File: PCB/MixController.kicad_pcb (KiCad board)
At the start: 2 copper layers, 150.2 x 114.3 mm, 120 parts, among them J11 B5B-XH-A(LF)(SN), J13 B8B-XH-A(LF)(SN), J2 B2B-XH-A(LF)(SN), J7 B3B-XH-A(LF)(SN), J9 B2B-XH-A(LF)(SN), J91 B4B-XH-A(LF)(SN), J94 0705430001, J95 B8B-XH-A(LF)(SN), J97 B4B-PH-K-S(LF)(SN), Q1 Q_NMOS_GDS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

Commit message: Continue Layout
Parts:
- added PS1: TMR_6-7215WIR, Local:TRACO_TMR_6, F.Cu at (187.3, 88.3)
- added PS2: RSDW20H-05, Local:RSDW20_H, F.Cu at (142.2, 58.4)
- added U2: Adafruit_1096, Local:Adafruit_1096, F.Cu at (214.0, 121.9)
- added U3: BOB-12009, Package_DIP:DIP-12_W10.16mm, F.Cu at (200.7, 63.5)
- added U4: BOB-12009, Package_DIP:DIP-12_W10.16mm, F.Cu at (96.5, 63.5)
- added U6: HSCDLNN001PDAA3, Local:HoneyWell_LN, F.Cu at (101.0, 90.8)
- moved R6 25.5 mm to (190.5, 45.7), turned to 0 degrees
- moved R2 20.8 mm to (179.1, 68.6), turned to 0 degrees
- moved R7 5.68 mm to (86.4, 45.7)
- moved R4 3.59 mm to (175.3, 132.1)
- moved R3 1.27 mm to (172.7, 128.3)
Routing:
- net /HARDENER_INPUT_A: track 0.00 -> 145.2 mm, vias 0 -> 2
- net /HARDENER_INPUT_B: track 0.00 -> 140.2 mm, vias 0 -> 2
- net /HARDENER_ENABLE: track 0.00 -> 44.5 mm
- net Net-(J84-Pad1): track 40.5 -> 1.50 mm
- net Net-(J83-Pad1): track 37.0 -> 0.00 mm
- net Net-(J13-Pad5): track 0.00 -> 19.8 mm
- net Net-(J95-Pad5): track 0.00 -> 19.8 mm
- net Net-(J13-Pad6): track 0.00 -> 19.8 mm
- net Net-(J95-Pad6): track 0.00 -> 19.8 mm
- net /HARDENER_HLFB: track 0.00 -> 19.5 mm
- net Net-(J95-Pad8): track 0.00 -> 17.9 mm
- net Net-(J13-Pad8): track 0.00 -> 17.9 mm
- net Net-(J95-Pad7): track 0.00 -> 17.9 mm
- net Net-(J13-Pad7): track 0.00 -> 17.9 mm
- net /USER_BUTTON: track 84.8 -> 86.3 mm
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
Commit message: Continue Layout
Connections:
- JP4 pad 1: /PAIL_SNS -> /PRESS_SNS
- JP5 pad 1: /PRESS_SNS -> /PAIL_SNS
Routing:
- net /RESIN_HLFB: track 0.00 -> 108.8 mm, vias 0 -> 4
- net /RESIN_ENABLE: track 0.00 -> 102.5 mm, vias 0 -> 4
- net /RESIN_INPUT_B: track 0.00 -> 101.2 mm, vias 0 -> 2
- net /HARDENER_HLFB: track 19.5 -> 120.2 mm, vias 0 -> 4
- net /RESIN_INPUT_A: track 0.00 -> 93.0 mm, vias 0 -> 2
- net /HARDENER_ENABLE: track 44.5 -> 130.8 mm, vias 0 -> 4
- net /PRESS_SNS: track 0.00 -> 54.8 mm
- net Net-(J84-Pad1): track 1.50 -> 41.8 mm
- net Net-(J83-Pad1): track 0.00 -> 37.0 mm
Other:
- board text added: "+5V"
- board text added: "3V3"
- board text added: "GND"

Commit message: Update Board Profile
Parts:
- moved PS2 138.5 mm to (5.71, 81.9)
- moved Q1 95.7 mm to (268.0, 46.4)
- moved R2 91.1 mm to (269.9, 61.6)
- moved PS1 66.7 mm to (121.3, 78.7), turned to 270 degrees
- moved J2 21.6 mm to (170.8, 57.1)
- moved J7 21.6 mm to (150.5, 57.1)
- moved J94 21.6 mm to (135.3, 57.1)
- moved JP10 10.9 mm to (146.1, 140.3)
- moved JP11 10.9 mm to (148.6, 140.3)
- moved JP19 10.9 mm to (128.3, 144.1)
- moved JP20 10.9 mm to (128.3, 146.7)
- moved JP23 10.9 mm to (128.3, 154.3)
- moved JP7 10.9 mm to (138.4, 140.3)
- moved JP8 10.9 mm to (141.0, 140.3)
- moved R9 10.9 mm to (181.6, 130.2)
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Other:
- board size 150.2 x 114.3 mm -> 150.2 x 127 mm

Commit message: Update PCB Layout
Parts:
- moved PS2 108.6 mm to (114.3, 80.0)
- moved Q1 102.9 mm to (169.5, 76.2), turned to 90 degrees
- moved R2 93.2 mm to (177.8, 76.2), turned to 270 degrees
- moved PS1 36.7 mm to (156.8, 87.6), turned to 0 degrees
- moved U6 6.35 mm to (97.2, 105.4)
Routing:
- net +5V: track 0.00 -> 486.5 mm, vias 0 -> 3
- net +3V3: track 0.00 -> 362.9 mm, vias 0 -> 6
- net +72V: track 0.00 -> 39.7 mm
- net +24V: track 0.00 -> 37.7 mm
- net Net-(J2-Pad2): track 0.00 -> 19.6 mm
- net /RESIN_HLFB: track 108.8 -> 121.5 mm
- net /RESIN_INPUT_B: track 101.2 -> 113.9 mm
- net /RESIN_INPUT_A: track 93.0 -> 105.7 mm
- net /RESIN_ENABLE: track 102.5 -> 115.2 mm
- net /HARDENER_INPUT_B: track 140.2 -> 152.9 mm
- net /HARDENER_INPUT_A: track 145.2 -> 157.9 mm
- net /HARDENER_ENABLE: track 130.8 -> 143.4 mm
- net /HARDENER_HLFB: track 120.2 -> 132.5 mm
- net /PRESS_SNS: track 54.8 -> 45.8 mm
- net /PUMP_EN: track 0.00 -> 8.26 mm
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
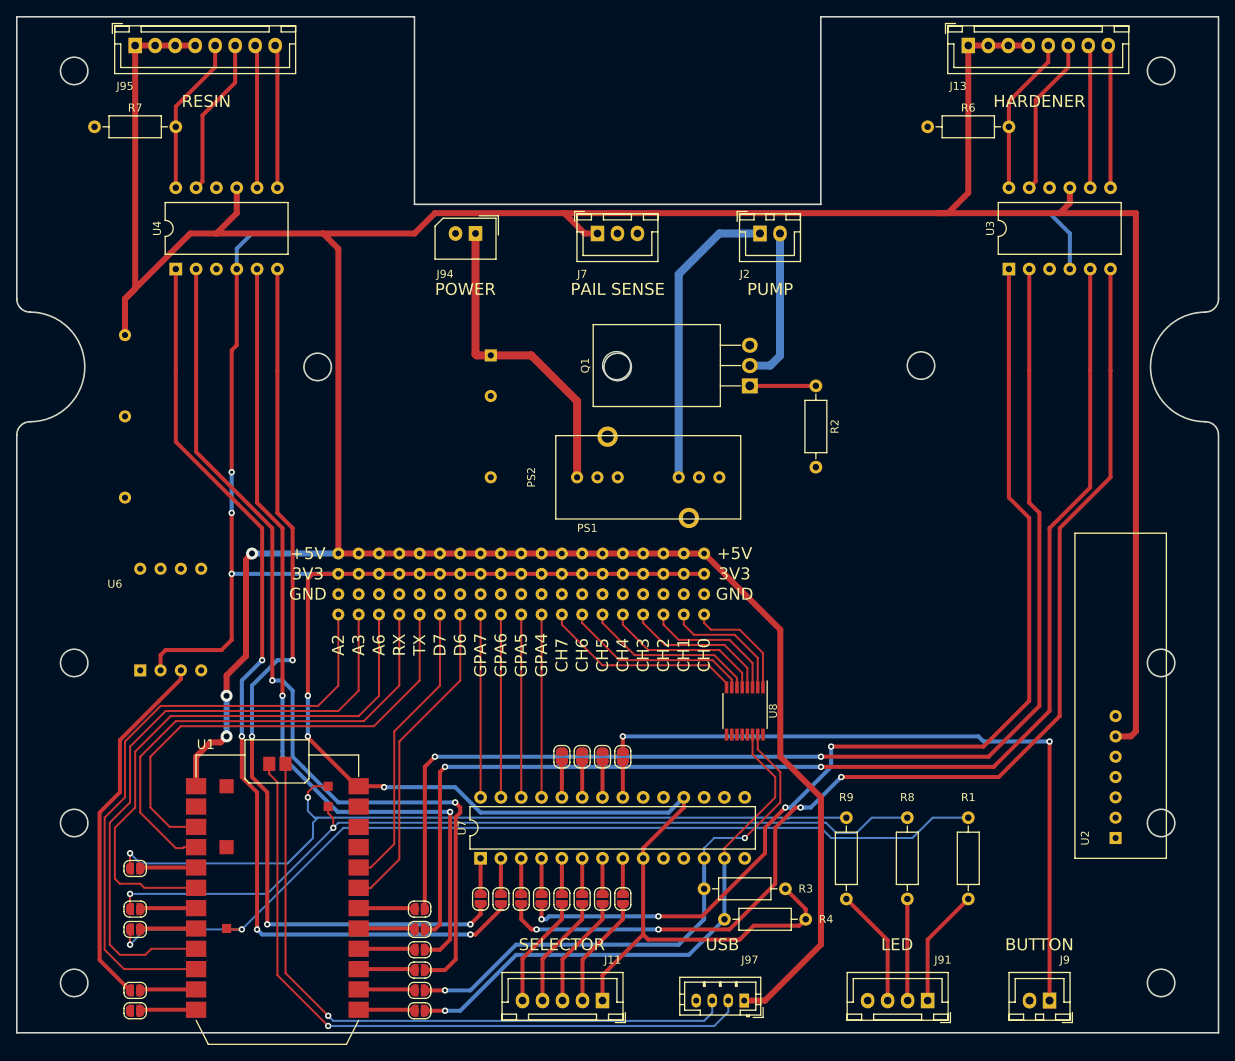
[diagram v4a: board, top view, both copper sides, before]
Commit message: Add indicator leds, chime speaker, update layout
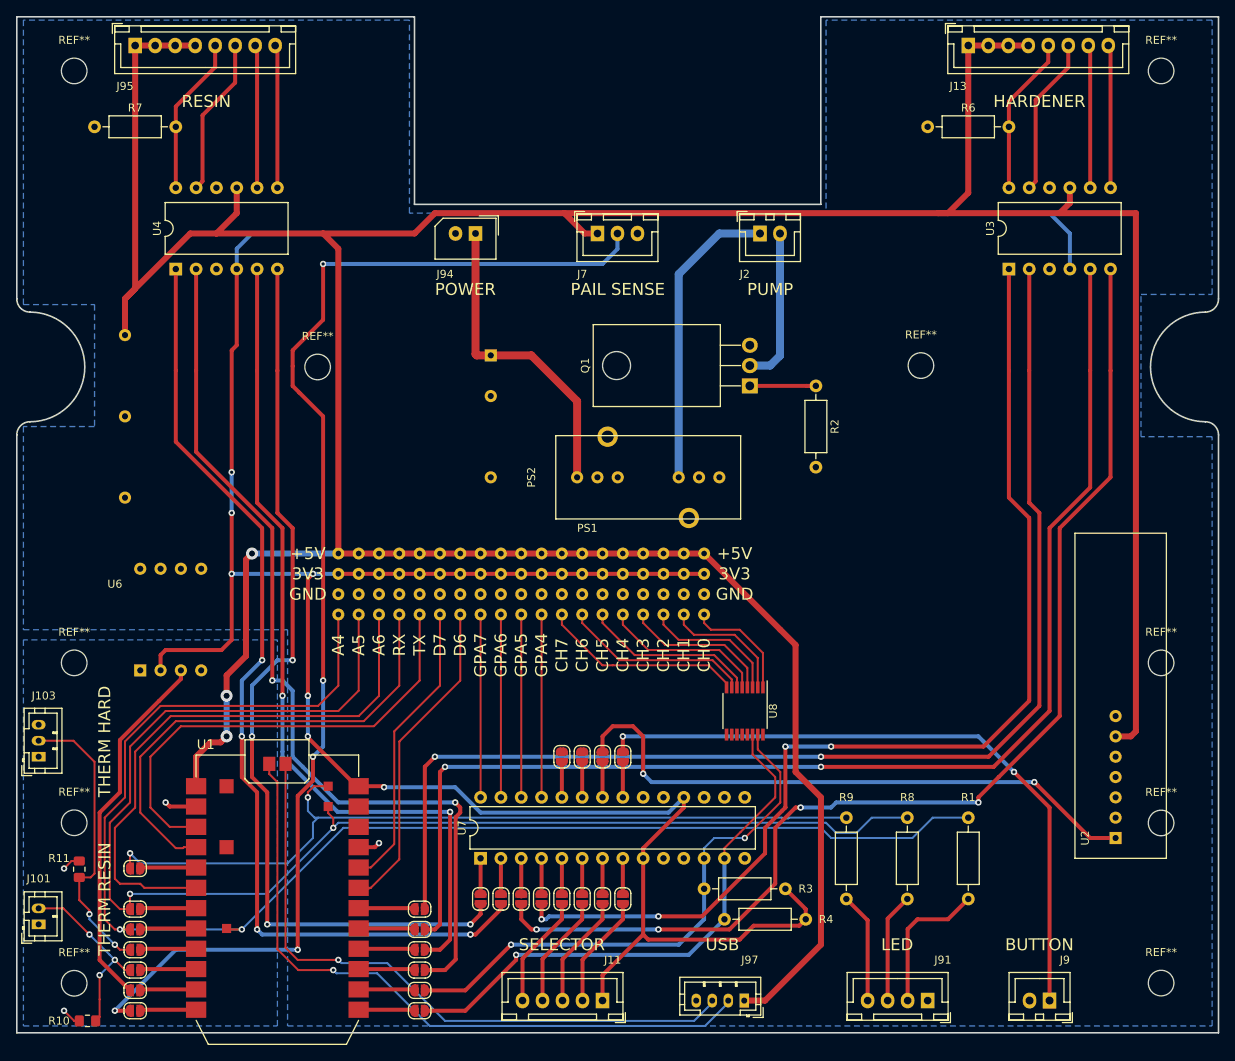
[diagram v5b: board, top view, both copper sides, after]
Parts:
- added J101: B2B-PH-K-S(LF)(SN), Connector_JST:JST_PH_B2B-PH-K_1x02_P2.00mm_Vertical, F.Cu at (80.6, 143.5)
- added J103: B3B-PH-K-S(LF)(SN), Connector_JST:JST_PH_B3B-PH-K_1x03_P2.00mm_Vertical, F.Cu at (80.6, 122.6)
- added JP24: ~, Jumper:SolderJumper-2_P1.3mm_Open_RoundedPad1.0x1.5mm, F.Cu at (92.7, 146.7)
- added JP25: ~, Jumper:SolderJumper-2_P1.3mm_Open_RoundedPad1.0x1.5mm, F.Cu at (92.7, 149.2)
- added R10: 10K .01%, Resistor_SMD:R_0805_2012Metric_Pad1.15x1.40mm_HandSolder, F.Cu at (86.8, 155.6)
- added R11: 10K .01%, Resistor_SMD:R_0805_2012Metric_Pad1.15x1.40mm_HandSolder, F.Cu at (85.7, 136.6)
- added REF**: MountingHole_3.2mm_M3_ISO7380, MountingHole:MountingHole_3.2mm_M3_ISO7380, F.Cu at (115.5, 73.8)
- added REF**: MountingHole_3.2mm_M3_ISO7380, MountingHole:MountingHole_3.2mm_M3_ISO7380, F.Cu at (85.1, 150.9)
- added REF**: MountingHole_3.2mm_M3_ISO7380, MountingHole:MountingHole_3.2mm_M3_ISO7380, F.Cu at (221.0, 110.8)
- added REF**: MountingHole_3.2mm_M3_ISO7380, MountingHole:MountingHole_3.2mm_M3_ISO7380, F.Cu at (221.0, 130.8)
- added REF**: MountingHole_3.2mm_M3_ISO7380, MountingHole:MountingHole_3.2mm_M3_ISO7380, F.Cu at (221.0, 150.9)
- added REF**: MountingHole_3.2mm_M3_ISO7380, MountingHole:MountingHole_3.2mm_M3_ISO7380, F.Cu at (190.9, 73.7)
- added REF**: MountingHole_3.2mm_M3_ISO7380, MountingHole:MountingHole_3.2mm_M3_ISO7380, F.Cu at (221.0, 36.8)
- added REF**: MountingHole_3.2mm_M3_ISO7380, MountingHole:MountingHole_3.2mm_M3_ISO7380, F.Cu at (85.1, 36.8)
- added REF**: MountingHole_3.2mm_M3_ISO7380, MountingHole:MountingHole_3.2mm_M3_ISO7380, F.Cu at (85.1, 110.8)
- added REF**: MountingHole_3.2mm_M3_ISO7380, MountingHole:MountingHole_3.2mm_M3_ISO7380, F.Cu at (85.1, 130.8)
- U7: value MCP23017 -> MCP23017_SP
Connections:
- J45 pad 1: Net-(J45-Pad1) -> /STATUS_LED_G
- J46 pad 1: Net-(J46-Pad1) -> /STATUS_LED_R
- J91 pad 1: Net-(J91-Pad1) -> +3V3
- J91 pad 4: GND -> Net-(J91-Pad4)
- R1 pad 2: Net-(J91-Pad1) -> Net-(J91-Pad2)
- R8 pad 2: Net-(J91-Pad2) -> Net-(J91-Pad3)
- R9 pad 2: Net-(J91-Pad3) -> Net-(J91-Pad4)
- U1 pad 10: Net-(J46-Pad1) -> Net-(JP25-Pad2)
- U1 pad 9: Net-(J45-Pad1) -> Net-(JP24-Pad2)
- U7 pad 11: (no net) -> Net-(U7-Pad11)
- U7 pad 14: (no net) -> Net-(U7-Pad14)
- U8 pad 11: Net-(U8-Pad11) -> GND
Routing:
- net /PAIL_SNS: track 0.00 -> 157.6 mm, vias 0 -> 5
- net Net-(J45-Pad1): track 78.4 -> 0.00 mm
- net Net-(J46-Pad1): track 78.0 -> 0.00 mm
- net /USER_REMOTE: track 0.00 -> 75.1 mm, vias 0 -> 2
- net /STATUS_LED_G: track 107.0 -> 171.1 mm
- net /STATUS_LED_R: track 116.3 -> 180.3 mm
- net /THERM_HARDENER: track 0.00 -> 36.6 mm, vias 0 -> 2
- net /THERM_RESIN: track 0.00 -> 23.2 mm, vias 0 -> 3
- net Net-(J91-Pad1): track 14.8 -> 0.00 mm
- net Net-(J91-Pad4): track 0.00 -> 13.8 mm
- net GND: track 0.00 -> 11.5 mm, vias 0 -> 4
- net Net-(JP24-Pad2): track 0.00 -> 7.00 mm
- net Net-(JP25-Pad2): track 0.00 -> 7.00 mm
- net Net-(J91-Pad2): track 12.7 -> 18.1 mm
- net /USER_BUTTON: track 87.9 -> 83.0 mm
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- added copper zone on B.Cu, net GND
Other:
- outline, holes or cut-outs redrawn
- board text added: "A4"
- board text added: "A5"
- board text added: "THERM HARD"
- board text added: "THERM RESIN"
- board text removed: "A2"
- board text removed: "A3"

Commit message: update schematic per ECN Maxx 5
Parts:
- added C1: 0.1u, Capacitor_SMD:C_0805_2012Metric_Pad1.15x1.40mm_HandSolder, F.Cu at (50.5, 146.1)
- added C2: 0.1u, Capacitor_SMD:C_0805_2012Metric_Pad1.15x1.40mm_HandSolder, F.Cu at (62.8, 136.2)
- added C3: 0.1u, Capacitor_SMD:C_0805_2012Metric_Pad1.15x1.40mm_HandSolder, F.Cu at (50.5, 148.0)
- added C4: 0.1u, Capacitor_SMD:C_0805_2012Metric_Pad1.15x1.40mm_HandSolder, F.Cu at (59.0, 139.3)
- added C5: 470u, Capacitor_SMD:C_0805_2012Metric_Pad1.15x1.40mm_HandSolder, F.Cu at (54.3, 146.1)
- added D10: STEP_HARD, LED_SMD:LED_0805_2012Metric_Pad1.15x1.40mm_HandSolder, F.Cu at (47.0, 113.6)
- added D11: STEP_RESIN, LED_SMD:LED_0805_2012Metric_Pad1.15x1.40mm_HandSolder, F.Cu at (39.4, 119.7)
- added D2: +72V, LED_SMD:LED_0805_2012Metric_Pad1.15x1.40mm_HandSolder, F.Cu at (39.4, 111.5)
- added D3: +5V, LED_SMD:LED_0805_2012Metric_Pad1.15x1.40mm_HandSolder, F.Cu at (39.4, 113.6)
- added D4: +24V, LED_SMD:LED_0805_2012Metric_Pad1.15x1.40mm_HandSolder, F.Cu at (43.2, 111.5)
- added D5: EN_HARD, LED_SMD:LED_0805_2012Metric_Pad1.15x1.40mm_HandSolder, F.Cu at (39.4, 115.6)
- added D6: EN_RESIN, LED_SMD:LED_0805_2012Metric_Pad1.15x1.40mm_HandSolder, F.Cu at (43.2, 113.6)
- added D7: PUMP, LED_SMD:LED_0805_2012Metric_Pad1.15x1.40mm_HandSolder, F.Cu at (47.0, 111.5)
- added D8: LIQ_RESIN, LED_SMD:LED_0805_2012Metric_Pad1.15x1.40mm_HandSolder, F.Cu at (39.4, 117.6)
- added D9: LIQ_HARD, LED_SMD:LED_0805_2012Metric_Pad1.15x1.40mm_HandSolder, F.Cu at (43.2, 115.6)
- added J104: B2B-XH-A(LF)(SN), Connector_JST:JST_XH_B02B-XH-A_1x02_P2.50mm_Vertical, F.Cu at (51.6, 141.2)
- added JP26: ~, Jumper:SolderJumper-2_P1.3mm_Open_RoundedPad1.0x1.5mm, F.Cu at (50.3, 152.2)
- added JP27: ~, Jumper:SolderJumper-2_P1.3mm_Open_RoundedPad1.0x1.5mm, F.Cu at (58.8, 143.5)
- added Q2: Q_NMOS_GDS, Package_TO_SOT_THT:TO-220-3_Horizontal_TabDown, F.Cu at (40.8, 155.0)
- added R12: 23k, Resistor_SMD:R_0805_2012Metric_Pad1.15x1.40mm_HandSolder, F.Cu at (50.7, 111.5)
- added R13: 1k, Resistor_SMD:R_0805_2012Metric_Pad1.15x1.40mm_HandSolder, F.Cu at (43.1, 117.6)
- added R14: 7k, Resistor_SMD:R_0805_2012Metric_Pad1.15x1.40mm_HandSolder, F.Cu at (46.9, 115.5)
- added R15: 100K, Resistor_SMD:R_0805_2012Metric_Pad1.15x1.40mm_HandSolder, F.Cu at (49.7, 136.8)
- added R16: 1k, Resistor_SMD:R_0805_2012Metric_Pad1.15x1.40mm_HandSolder, F.Cu at (50.7, 113.4)
- added R17: 1k, Resistor_SMD:R_0805_2012Metric_Pad1.15x1.40mm_HandSolder, F.Cu at (43.1, 119.5)
- added R18: 7k, Resistor_SMD:R_0805_2012Metric_Pad1.15x1.40mm_HandSolder, F.Cu at (46.9, 117.5)
- added R19: 10k, Resistor_SMD:R_0805_2012Metric_Pad1.15x1.40mm_HandSolder, F.Cu at (59.0, 141.2)
- added R20: 10k, Resistor_SMD:R_0805_2012Metric_Pad1.15x1.40mm_HandSolder, F.Cu at (62.8, 138.2)
- added R21: 470, Resistor_SMD:R_0805_2012Metric_Pad1.15x1.40mm_HandSolder, F.Cu at (50.5, 150.0)
- added R22: 470, Resistor_SMD:R_0805_2012Metric_Pad1.15x1.40mm_HandSolder, F.Cu at (66.6, 136.2)
- added R23: 1k, Resistor_SMD:R_0805_2012Metric_Pad1.15x1.40mm_HandSolder, F.Cu at (50.7, 115.5)
- added R24: 1k, Resistor_SMD:R_0805_2012Metric_Pad1.15x1.40mm_HandSolder, F.Cu at (46.9, 119.4)
- added TP1: SCL, TestPoint:TestPoint_THTPad_D1.5mm_Drill0.7mm, F.Cu at (53.7, 148.3)
- added TP2: SDA, TestPoint:TestPoint_THTPad_D1.5mm_Drill0.7mm, F.Cu at (57.4, 146.4)
- J38: value ~ -> B5B-PH-K-S(LF)(SN); footprint Local:ConnectorPoint_THT_D1.5mm_Drill-0.7mm -> Connector_JST:JST_PH_B5B-PH-K_1x05_P2.00mm_Vertical
- J55: value ~ -> PHR-5
- J67: value ~ -> B6B-PH-K-S(LF)(SN); footprint Local:ConnectorPoint_THT_D1.5mm_Drill-0.7mm -> Connector_JST:JST_PH_B6B-PH-K_1x06_P2.00mm_Vertical
- J71: value ~ -> PHR-6
- R10, R11: value 10K .01% -> 5K .01%
- R2: footprint Resistor_THT:R_Axial_DIN0207_L6.3mm_D2.5mm_P10.16mm_Horizontal -> Resistor_SMD:R_0805_2012Metric_Pad1.15x1.40mm_HandSolder
- moved J67 108.7 mm to (36.1, 85.4), turned to 0 degrees
- moved J38 107.6 mm to (36.1, 91.0), turned to 0 degrees
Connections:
- net /HARDENER_INPUT_A renamed /HARDENER_INPUT_DIR
- net /HARDENER_INPUT_B renamed /HARDENER_INPUT_STEP
- J43 pad 1: Net-(J43-Pad1) -> /CHIME
- J55 pad 1: +3V3 -> Net-(J55-Pad1)
- J67 pad 1: GND -> +5V
- JP17 pad 1: /LIQUID_SENSE -> /LIQUID_SNS_RESIN
- JP20 pad 2: /RESIN_INPUT_A -> /RESIN_INPUT_STEP
- JP21 pad 2: /RESIN_INPUT_B -> /RESIN_INPUT_DIR
- U1 pad 4: Net-(J43-Pad1) -> Net-(JP26-Pad2)
- U4 pad 2: /RESIN_INPUT_B -> /RESIN_INPUT_STEP
- U4 pad 5: /RESIN_INPUT_A -> /RESIN_INPUT_DIR
- U7 pad 25: Net-(J71-Pad1) -> Net-(JP27-Pad2)

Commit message: Update Layout
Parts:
- removed J55: PHR-5, Local:ConnectorPoint_THT_D1.5mm_Drill-0.7mm
- removed J71: PHR-6, Local:ConnectorPoint_THT_D1.5mm_Drill-0.7mm
- R1, R3, R4, R6, R7, R8, R9: footprint Resistor_THT:R_Axial_DIN0207_L6.3mm_D2.5mm_P10.16mm_Horizontal -> Resistor_SMD:R_0805_2012Metric_Pad1.15x1.40mm_HandSolder
- moved D5 190.1 mm to (215.9, 45.1)
- moved R16 177.6 mm to (215.9, 48.3)
- moved D10 172.7 mm to (205.5, 45.1)
- moved R23 168.8 mm to (205.5, 48.3)
- moved D9 158.9 mm to (199.8, 88.9)
- moved J67 155.4 mm to (189.9, 108.0)
- moved D8 154.4 mm to (191.1, 88.9)
- moved J38 153.9 mm to (189.9, 99.1)
- moved R21 152.1 mm to (191.1, 92.1), turned to 180 degrees
- moved Q2 144.8 mm to (184.2, 134.0)
- moved R18 141.6 mm to (179.3, 67.3), turned to 180 degrees
- moved D4 141.3 mm to (182.6, 88.9)
- moved R22 140.3 mm to (199.8, 92.1), turned to 180 degrees
- moved D7 138.6 mm to (179.3, 70.5)
- moved R14 137.7 mm to (182.6, 92.1), turned to 180 degrees
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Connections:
- JP16 pad 1: /PUMP_EN -> /LIQUID_SNS_HARDENER
- JP27 pad 1: /LIQUID_SNS_HARDENER -> /PUMP_EN
- R23 pad 1: Net-(J13-Pad5) -> Net-(J13-Pad6)
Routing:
- net +3V3: track 359.8 -> 517.7 mm, vias 7 -> 13
- net /CHIME: track 0.00 -> 138.7 mm, vias 0 -> 3
- net /RESIN_INPUT_B: track 113.9 -> 0.00 mm, vias 2 -> 0
- net /RESIN_INPUT_DIR: track 0.00 -> 110.0 mm, vias 0 -> 2
- net /RESIN_INPUT_STEP: track 0.00 -> 108.9 mm, vias 0 -> 2
- net /RESIN_INPUT_A: track 105.7 -> 0.00 mm, vias 2 -> 0
- net /LIQUID_SNS_HARDENER: track 0.00 -> 79.2 mm, vias 0 -> 2
- net /PUMP_EN: track 8.26 -> 85.2 mm, vias 0 -> 2
- net /LIQUID_SNS_RESIN: track 0.00 -> 74.7 mm, vias 0 -> 3
- net Net-(J43-Pad1): track 60.8 -> 0.00 mm
- net +5V: track 486.5 -> 546.1 mm, vias 3 -> 5
- net GND: track 11.5 -> 51.3 mm, vias 4 -> 19
- net +24V: track 37.7 -> 76.4 mm, vias 0 -> 1
- net Net-(J104-Pad2): track 0.00 -> 26.6 mm, vias 0 -> 1
- net Net-(J71-Pad1): track 22.9 -> 0.00 mm
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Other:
- rule trace_min: 0.2 -> 0.1524
- rule via_min_size: 0.4 -> 0.28194
- board text added: "CHIME"
- board text added: "LIQUID HARD"
- board text added: "LIQUID RESIN"
- board text removed: "GPA4"

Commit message: Finalize layout for v0.0.15
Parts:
- removed the REF** at (115.5, 73.8)
- removed the REF** at (190.9, 73.7)
- added R25: 2.2k, Resistor_SMD:R_0805_2012Metric_Pad1.15x1.40mm_HandSolder, F.Cu at (87.6, 99.9)
- added R26: 4.7k, Resistor_SMD:R_0805_2012Metric_Pad1.15x1.40mm_HandSolder, F.Cu at (83.8, 99.9)
- PS1: value TMR_6-7215WIR -> ERM01H110; footprint Local:TRACO_TMR_6 -> VDW-Modules:ERM01H110
- PS2: footprint Local:RSDW20_H -> VDW-Modules:RSDW20_H
- U6: value HSCDLNN001PDAA3 -> HSCDANN005PGAA5; footprint Local:HoneyWell_LN -> VDW-Modules:HoneyWell_DIP_AN
- moved Q1 23.5 mm to (169.5, 52.7)
- moved R18 23.5 mm to (179.3, 43.8)
- moved R2 23.5 mm to (179.3, 52.7)
- moved D7 23.5 mm to (179.3, 47.0)
- moved J2 23.5 mm to (170.8, 33.7)
- moved J7 23.5 mm to (150.5, 33.7)
- moved J94 23.5 mm to (135.3, 33.7)
- moved PS1 22.0 mm to (171.4, 71.1)
- moved D3 21.6 mm to (152.4, 88.9)
- moved D4 21.6 mm to (161.0, 88.9)
- moved R13 21.6 mm to (152.4, 92.1)
- moved R14 21.6 mm to (161.1, 92.1)
- moved R12 14.6 mm to (125.1, 48.3)
- moved D2 14.6 mm to (125.1, 45.1)
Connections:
- PS1 pad 6: +24V -> GND
- U6 pad 2: +3V3 -> +5V
- U6 pad 3: /PRESS_SNS -> Net-(R25-Pad1)
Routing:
- net +3V3: track 517.7 -> 440.2 mm
- net /PUMP_EN: track 85.2 -> 116.3 mm
- net +24V: track 76.4 -> 105.8 mm
- net +5V: track 546.1 -> 572.5 mm, vias 5 -> 4
- net +72V: track 54.3 -> 78.7 mm
- net /PAIL_SNS: track 151.0 -> 174.5 mm, vias 5 -> 6
- net Net-(R25-Pad1): track 0.00 -> 18.7 mm
- net GND: track 51.3 -> 65.4 mm, vias 19 -> 20
- net /PRESS_SNS: track 49.2 -> 61.9 mm
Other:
- outline, holes or cut-outs redrawn
- board text added: "Mix Controller v0.0.15 Veenema Design Works ben@veenemadesignworks.com"
